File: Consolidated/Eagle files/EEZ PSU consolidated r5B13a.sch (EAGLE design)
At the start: 551 parts, among them IC1 LTC3864EMSE#PBF, IC10 DAC8552IDGKTG4, IC11 ADG465SOT-23, IC12 TS5A9411DCKT, IC13 ADS1120IPWR, IC14 LP339D, IC15 TPD4E002DRL, IC16 TPD2E001DZDR, IC17 ADUM3160BRWZ, IC18 TLC5925IDBQR, IC19 Si8641EC-B-IS1, IC2 LP2951SO8, IC20 SI8651EC-B-IS1, IC21 SI8651EC-B-IS1, IC22 LD1117ADT33TR, IC23 Si8641EC-B-IS1, IC24 PCA21125T/Q900/1,1, IC25 AT25256B-SSHL-B, IC26 W5500, IC27 BC857BS, IC28 TLC555, IC29 SN74LVC08APWR, IC3 TL783CKTTR, IC30 SN74LV1T34DBVR, IC31 TPS3705-33D, IC32 SN74LVC2G02DCTR, IC33 74LVC1G125GW.125, IC34 TPA6205A1DGN, IC4 LTC3260EMSE#PBF, IC5 TL072D, IC6 TL072D, IC7 LTC2050HVCS8#PBF, IC8 MCP23S17-E/SS, IC9 REF5025AIDG4, J1 BS-244DSM-R, J2 1-726388-2, J3 BS-244DSM-G, J4 BS-244DSM-B, J5 BS-244DSM-R, J6 BS-244DSM-B, J7 693072010801, Q1 IRFR5305, Q10 MMBT5401, Q11 MMBT5551, Q12 MMBT5551, Q13 IRLL2705PBF, Q14 IRFR48ZPBF, Q15 IRLML2246TRPBF, Q16 2N7002, Q17 MMBT5551, Q18 MMBT5401, Q19 MMBT5551, Q2 MMBT5401, Q20 MMBT5551, Q21 BTA26-600, Q22 BTA26-600, Q23 IRLL2705PBF, Q24 2N7002, Q25 2N7002, Q26 IRLML2246TRPBF, Q27 IRLML2246TRPBF, Q28 IRLML2246TRPBF, Q29 IRLML2246TRPBF, Q3 2N7002, Q30 2N7002, Q31 IRLML2246TRPBF, Q32 2N7002, Q33 2N7002, Q34 2N7002, Q4 IRFP250N, Q5 BC857C, Q6 BCP56-16.115, Q7 IRFR5305, Q8 BCP56-16.115, Q9 MMBT5401, SW1 A101SYCQ04, SW2 PEC12R-4225F-S0024, SW3 1301.9316, X1 39-30-1039, X10 826629-5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

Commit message: r5B13a Eagle files
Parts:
- removed JP5, JP6, JP7, JP8: 0R-JUMPA, jump-0r-smd:0R-JUMPA
- added C156: 1u, rcl:C-EUC0805
- added R178: 100K, rcl:R-EU_R0805
- R160: value n.c. -> 100K
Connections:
- removed net N$104: JP7-0R.2, LCD1.T_DO
- removed net N$105: JP5-0R.2, LCD1.T_CLK
- removed net N$106: JP6-0R.2, LCD1.T_DIN
- net !MR: now also IC31.!WDO; no longer JP8-0R.1
- net !RESET: now also R160.1
- net +3V3: no longer R160.2
- net GND: now also C156.2, R178.2; no longer IC31.PFI
- net MISO: no longer JP7-0R.1
- net MOSI: no longer JP6-0R.1
- net N$151: now also C156.1, IC31.PFI, R160.2, R178.1; no longer IC31.!WDO, JP8-0R.2
- net N$185: now also IC31.!PFO; no longer JP8-0R.3, R160.1
- net SCLK: no longer JP5-0R.1
- net TOUCH_DIN: now also LCD1.T_DIN; no longer JP6-0R.3
- net TOUCH_DOUT: now also LCD1.T_DO; no longer JP7-0R.3
- net TOUCH_SCLK: now also LCD1.T_CLK; no longer JP5-0R.3
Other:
- note added: "EEZ PSU consolidated r5B13a - Sheet: 3/12"
- note removed: "EEZ PSU consolidated r5B13 - Sheet: 3/12"
- moved on the sheet: C139, C140, D21, IC31, R160

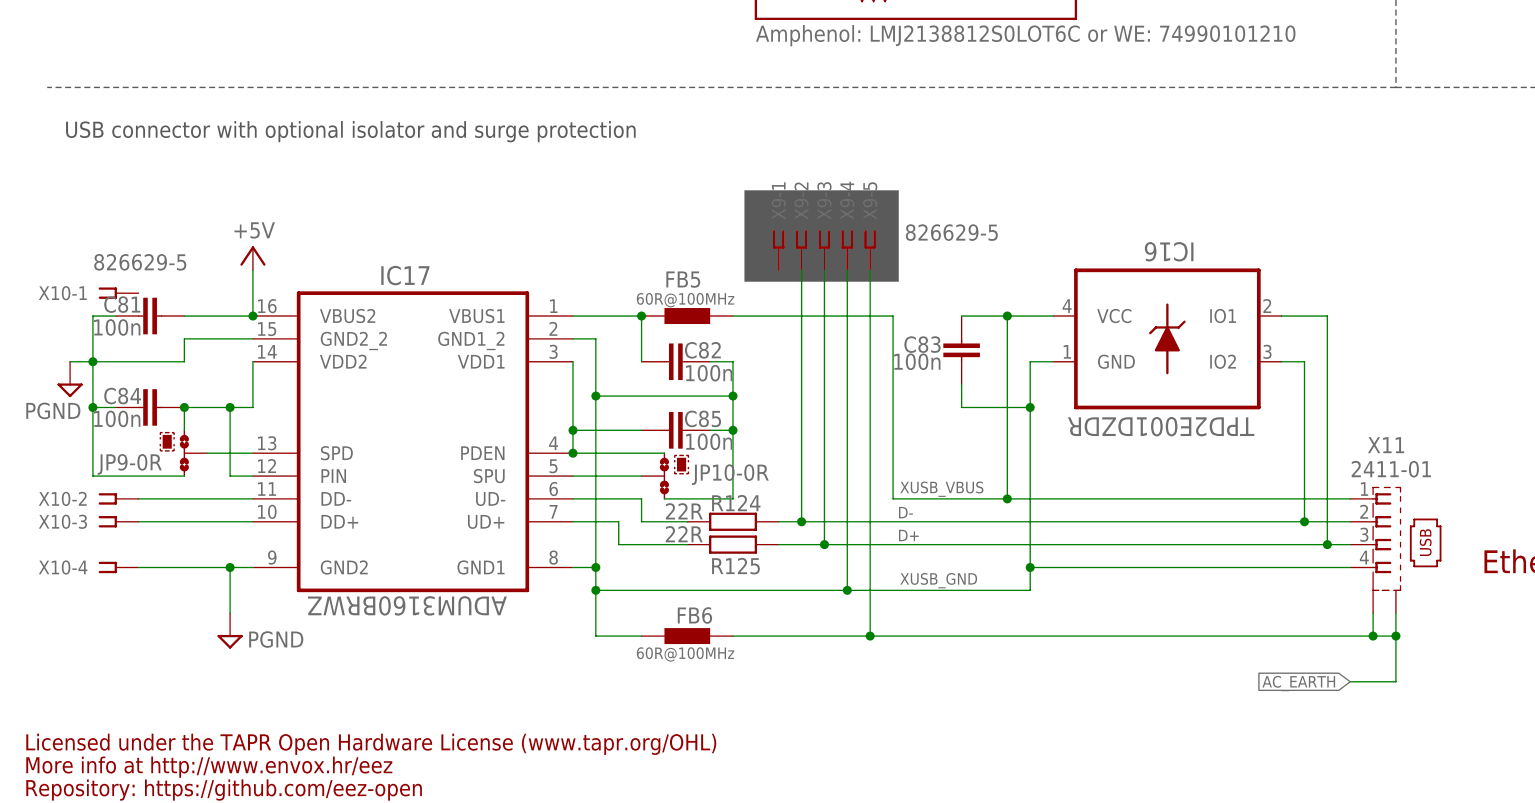
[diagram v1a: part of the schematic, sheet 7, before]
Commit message: JP9, JP10 changed to THT
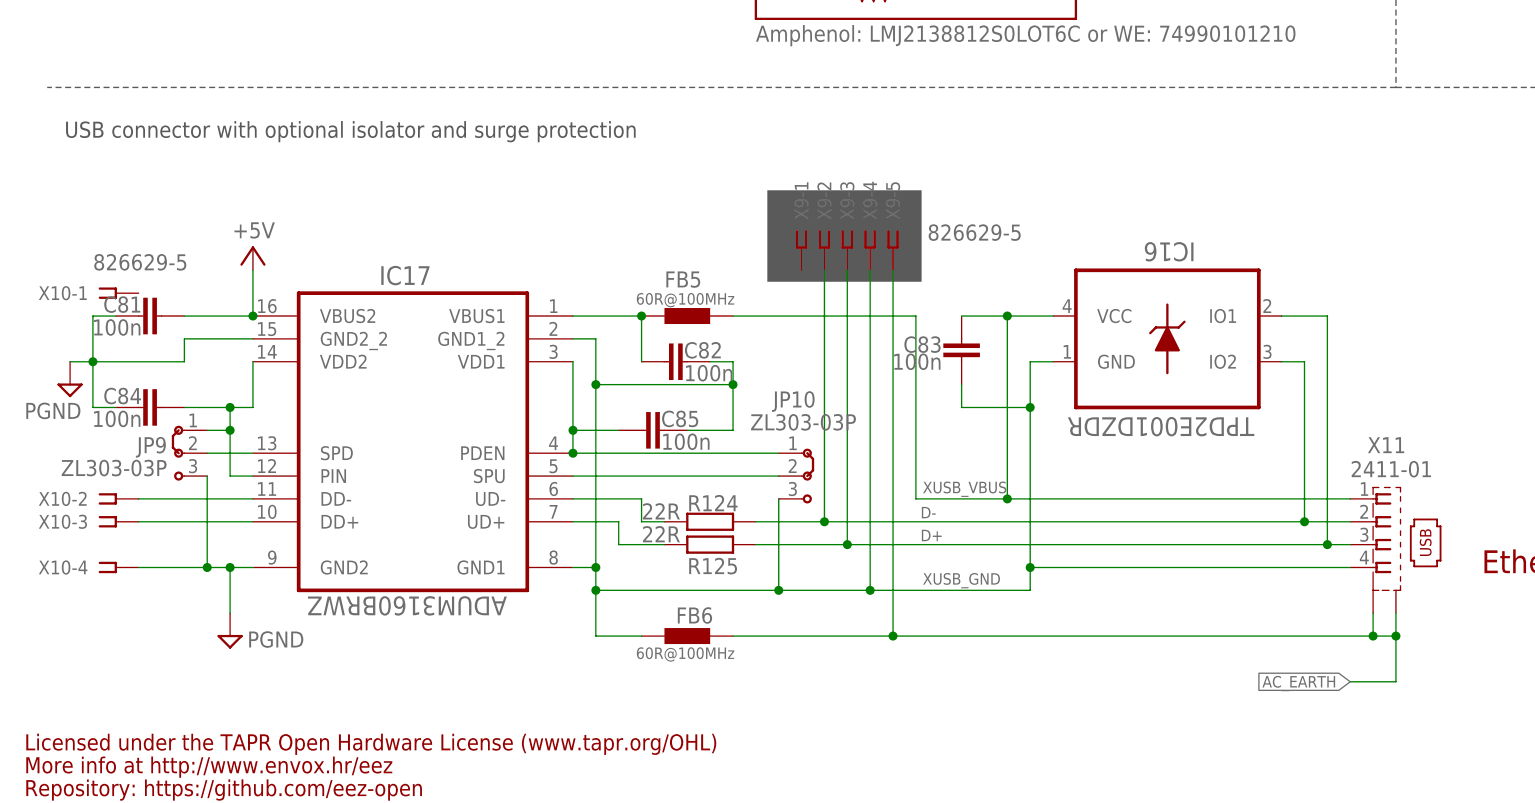
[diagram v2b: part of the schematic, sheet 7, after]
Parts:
- JP10, JP9: value 0R-JUMPA -> ZL303-03P; device jump-0r-smd:0R-JUMPA -> EEZ_Lib1:JUMPER-3PIN2MM
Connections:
- net GND: now also JP9.3; no longer JP9-0R.3
- net N$125: now also JP10.2; no longer JP10-0R.2
- net N$54: now also JP9.2; no longer JP9-0R.2
- net N$87: now also JP10.1; no longer JP10-0R.1
- net N$91: now also JP9.1; no longer JP9-0R.1
- net XUSB_GND: now also JP10.3; no longer JP10-0R.3
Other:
- note added: "1-2"
- note added: "2-3"
- note added: "High"
- note added: "JP9, JP10"
- note added: "Low"
- note added: "USB speed"
- moved on the sheet: C85, R124, R125, X9-1, X9-2, X9-3, X9-4, X9-5

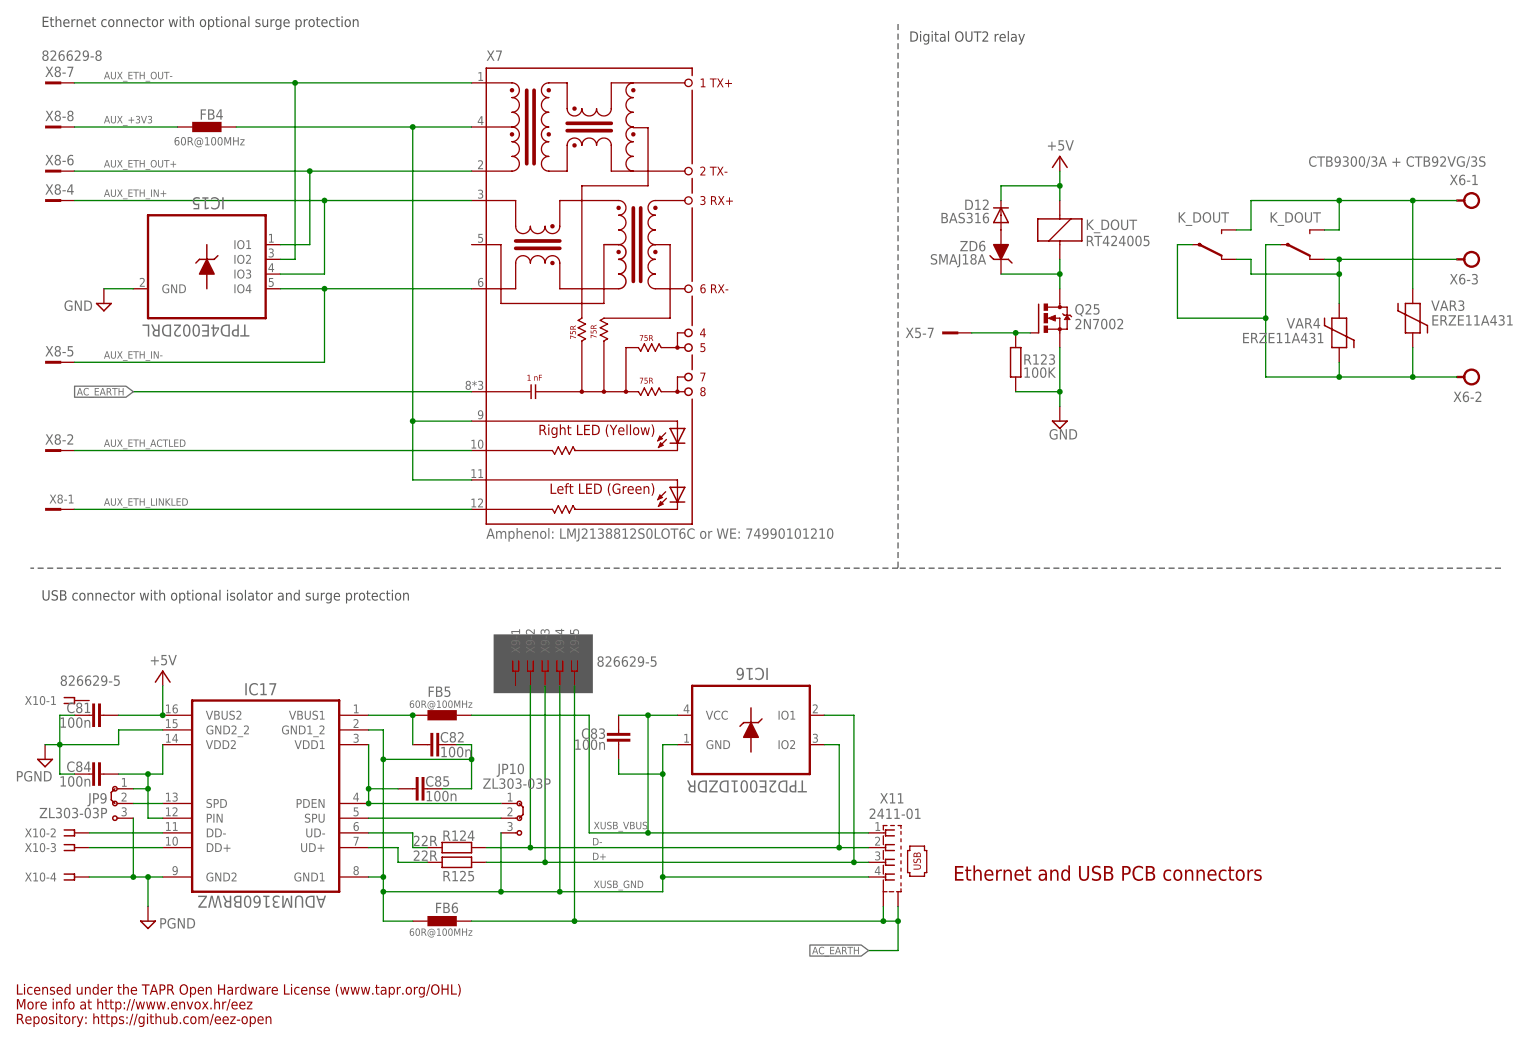
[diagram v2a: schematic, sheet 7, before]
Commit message: X1 holes adjustment
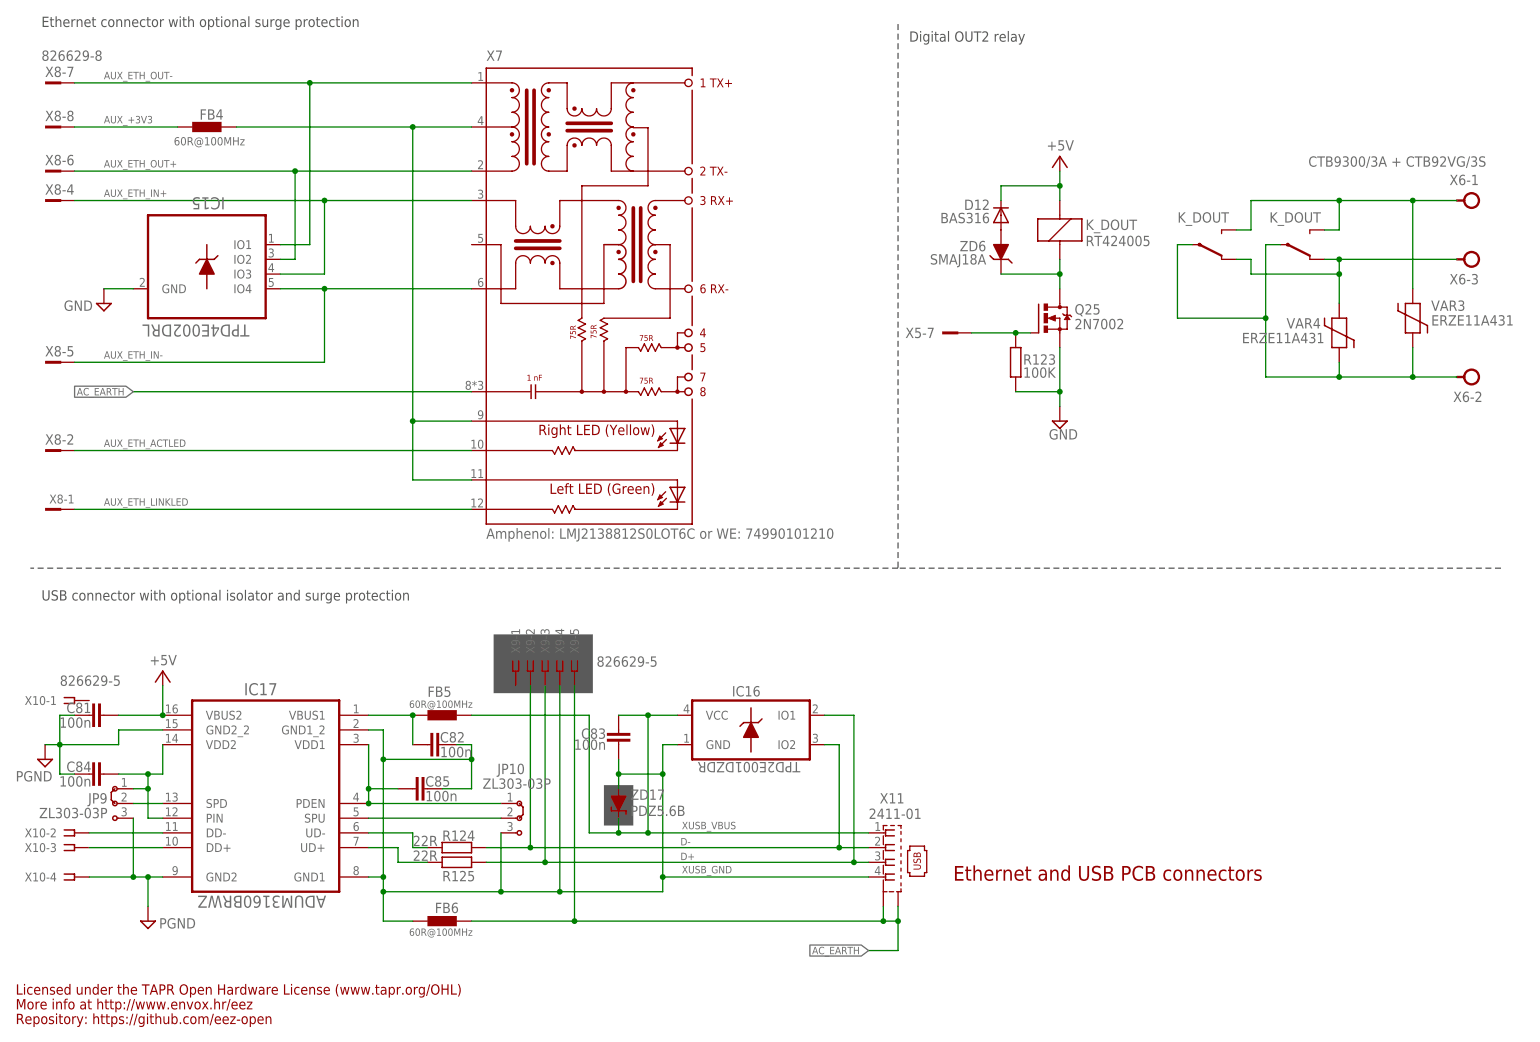
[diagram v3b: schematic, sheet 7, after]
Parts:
- added ZD17: PDZ5.6B, EEZ_Lib1:ZENER-DIODESOD323
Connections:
- net AC_IN1: now also ZD15.A; no longer ZD15.2
- net AC_IN2: now also ZD15.C; no longer ZD15.1
- net AUX_ETH_OUT+: now also IC15.IO2; no longer IC15.IO1
- net AUX_ETH_OUT-: now also IC15.IO1; no longer IC15.IO2
- net DC_OUT: now also ZD1.C; no longer ZD1.1
- net GND: now also ZD1.A; no longer ZD1.2
- net XUSB_GND: now also ZD17.A
- net XUSB_VBUS: now also ZD17.C
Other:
- note added: "Mount Q21 and Q22 on KK1"
- note removed: "Mount Q20 and Q21 on KK1"
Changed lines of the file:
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@@
 <part name="JP9" library="EEZ_Lib1" deviceset="JUMPER-3PIN" device="2MM" value="ZL303-03P"/>
 <part name="JP10" library="EEZ_Lib1" deviceset="JUMPER-3PIN" device="2MM" value="ZL303-03P"/>
+<part name="ZD17" library="EEZ_Lib1" deviceset="ZENER-DIODE" device="SOD323" value="PDZ5.6B"/>
 </parts>
 <sheets>
@@
 </segment>
 <segment>
-<pinref part="ZD1" gate="G$1" pin="2"/>
+<pinref part="ZD1" gate="G$1" pin="A"/>
 <wire x1="114.3" y1="160.02" x2="111.76" y2="160.02" width="0.4064" layer="91"/>
 <wire x1="111.76" y1="160.02" x2="111.76" y2="157.48" width="0.4064" layer="91"/>
@@
 <wire x1="129.54" y1="144.78" x2="124.46" y2="144.78" width="0.4064" layer="91"/>
 <junction x="124.46" y="144.78"/>
-<pinref part="ZD1" gate="G$1" pin="1"/>
+<pinref part="ZD1" gate="G$1" pin="C"/>
 <wire x1="121.92" y1="160.02" x2="124.46" y2="160.02" width="0.4064" layer="91"/>
 <pinref part="L1" gate="-1" pin="2"/>
@@
 <text x="88.265" y="107.95" size="1.778" layer="97" rot="MR180">+12VDC fan control</text>
 <wire x1="86.36" y1="43.18" x2="86.36" y2="109.22" width="0.1524" layer="97" style="shortdash"/>
-<text x="146.05" y="166.37" size="1.6764" layer="103">Mount Q20 and Q21 on KK1</text>
+<text x="146.05" y="166.37" size="1.6764" layer="103">Mount Q21 and Q22 on KK1</text>
 <text x="184.785" y="107.95" size="1.778" layer="97" rot="MR180">Fan sense (tacho out)</text>
 <wire x1="182.88" y1="38.1" x2="182.88" y2="109.22" width="0.1524" layer="97" style="shortdash"/>
@@
 <text x="34.925" y="70.485" size="1.6764" layer="103">USB speed</text>
 <text x="38.1" y="64.77" size="1.6764" layer="103">Low</text>
+<rectangle x1="104.14" y1="36.83" x2="109.22" y2="43.815" layer="97"/>
 </plain>
 <instances>
@@
 </instance>
 <instance part="IC16" gate="A" x="129.54" y="53.34" smashed="yes" rot="MR0">
-<attribute name="NAME" x="126.873" y="64.0588" size="2.0828" layer="95" ratio="10" rot="SMR180"/>
-<attribute name="VALUE" x="118.4148" y="44.6278" size="2.0828" layer="96" ratio="10" rot="SMR180"/>
+<attribute name="NAME" x="126.238" y="59.1312" size="1.778" layer="95" ratio="10" rot="SR0"/>
+<attribute name="VALUE" x="120.3198" y="47.8028" size="1.778" layer="96" ratio="10" rot="SMR180"/>
 </instance>
 <instance part="SUPPLY48" gate="GND" x="17.78" y="127" smashed="yes" rot="MR0">
@@
 <attribute name="VALUE" x="83.185" y="43.18" size="1.778" layer="96"/>
 </instance>
+<instance part="ZD17" gate="G$1" x="106.68" y="40.64" smashed="yes" rot="R270">
+<attribute name="NAME" x="108.712" y="41.275" size="1.778" layer="95"/>
+<attribute name="VALUE" x="108.712" y="38.481" size="1.778" layer="96"/>
+</instance>
 </instances>
 <busses>
@@
 <net name="D-" class="0">
 <segment>
-<label x="102.108" y="33.401" size="1.27" layer="102"/>
+<label x="117.348" y="33.401" size="1.27" layer="102"/>
 <pinref part="R124" gate="G$1" pin="1"/>
 <wire x1="83.82" y1="33.02" x2="91.44" y2="33.02" width="0.1524" layer="91"/>
@@
 <net name="D+" class="0">
 <segment>
-<label x="102.108" y="30.861" size="1.27" layer="102"/>
+<label x="117.348" y="30.861" size="1.27" layer="102"/>
 <pinref part="R125" gate="G$1" pin="1"/>
 <wire x1="83.82" y1="30.48" x2="93.98" y2="30.48" width="0.1524" layer="91"/>
@@
 <net name="XUSB_VBUS" class="0">
 <segment>
-<label x="102.362" y="36.195" size="1.27" layer="102"/>
+<label x="117.602" y="36.195" size="1.27" layer="102"/>
 <pinref part="FB5" gate="G$1" pin="1"/>
 <pinref part="X11" gate="G$1" pin="1"/>
@@
 <wire x1="111.76" y1="55.88" x2="106.68" y2="55.88" width="0.1524" layer="91"/>
 <junction x="111.76" y="55.88"/>
-<wire x1="111.76" y1="35.56" x2="101.6" y2="35.56" width="0.1524" layer="91"/>
+<wire x1="111.76" y1="35.56" x2="106.68" y2="35.56" width="0.1524" layer="91"/>
+<wire x1="106.68" y1="35.56" x2="101.6" y2="35.56" width="0.1524" layer="91"/>
 <wire x1="101.6" y1="35.56" x2="101.6" y2="55.88" width="0.1524" layer="91"/>
 <pinref part="C83" gate="G$1" pin="2"/>
+<wire x1="106.68" y1="38.1" x2="106.68" y2="35.56" width="0.1524" layer="91"/>
+<junction x="106.68" y="35.56"/>
+<pinref part="ZD17" gate="G$1" pin="C"/>
 </segment>
 </net>
@@
 <junction x="66.04" y="48.26"/>
 <wire x1="66.04" y1="20.32" x2="66.04" y2="25.4" width="0.1524" layer="91"/>
-<label x="102.362" y="26.035" size="1.27" layer="102"/>
+<label x="117.602" y="28.575" size="1.27" layer="102"/>
 <pinref part="X9" gate="-4" pin="1"/>
 <pinref part="X11" gate="G$1" pin="4"/>
@@
 <wire x1="86.36" y1="35.56" x2="86.36" y2="25.4" width="0.1524" layer="91"/>
 <junction x="86.36" y="25.4"/>
+<wire x1="106.68" y1="43.18" x2="106.68" y2="45.72" width="0.1524" layer="91"/>
+<junction x="106.68" y="45.72"/>
+<pinref part="ZD17" gate="G$1" pin="A"/>
 </segment>
 </net>
 <net name="AUX_ETH_OUT-" class="0">
 <segment>
-<wire x1="81.28" y1="165.1" x2="50.8" y2="165.1" width="0.1524" layer="91"/>
 <pinref part="X7" gate="G$1" pin="TD+"/>
-<wire x1="50.8" y1="165.1" x2="12.7" y2="165.1" width="0.1524" layer="91"/>
-<wire x1="50.8" y1="134.62" x2="50.8" y2="165.1" width="0.1524" layer="91"/>
-<junction x="50.8" y="165.1"/>
+<wire x1="81.28" y1="165.1" x2="53.34" y2="165.1" width="0.1524" layer="91"/>
 <label x="17.78" y="165.735" size="1.27" layer="102"/>
 <pinref part="X8" gate="-7" pin="1"/>
-<pinref part="IC15" gate="A" pin="IO2"/>
-<wire x1="48.26" y1="134.62" x2="50.8" y2="134.62" width="0.1524" layer="91"/>
+<pinref part="IC15" gate="A" pin="IO1"/>
+<wire x1="53.34" y1="165.1" x2="12.7" y2="165.1" width="0.1524" layer="91"/>
+<wire x1="48.26" y1="137.16" x2="53.34" y2="137.16" width="0.1524" layer="91"/>
+<wire x1="53.34" y1="137.16" x2="53.34" y2="165.1" width="0.1524" layer="91"/>
+<junction x="53.34" y="165.1"/>
 </segment>
 </net>
@@
 <segment>
 <pinref part="X7" gate="G$1" pin="TD-"/>
-<wire x1="12.7" y1="149.86" x2="53.34" y2="149.86" width="0.1524" layer="91"/>
-<wire x1="53.34" y1="149.86" x2="81.28" y2="149.86" width="0.1524" layer="91"/>
-<junction x="53.34" y="149.86"/>
+<wire x1="12.7" y1="149.86" x2="50.8" y2="149.86" width="0.1524" layer="91"/>
 <label x="17.78" y="150.495" size="1.27" layer="102"/>
 <pinref part="X8" gate="-6" pin="1"/>
-<pinref part="IC15" gate="A" pin="IO1"/>
-<wire x1="53.34" y1="137.16" x2="53.34" y2="149.86" width="0.1524" layer="91"/>
-<wire x1="48.26" y1="137.16" x2="53.34" y2="137.16" width="0.1524" layer="91"/>
+<pinref part="IC15" gate="A" pin="IO2"/>
+<wire x1="50.8" y1="149.86" x2="81.28" y2="149.86" width="0.1524" layer="91"/>
+<wire x1="48.26" y1="134.62" x2="50.8" y2="134.62" width="0.1524" layer="91"/>
+<wire x1="50.8" y1="134.62" x2="50.8" y2="149.86" width="0.1524" layer="91"/>
+<junction x="50.8" y="149.86"/>
 </segment>
 </net>
@@
 <pinref part="R163" gate="G$1" pin="1"/>
 <pinref part="IC30" gate="A" pin="I"/>
+<wire x1="162.56" y1="86.36" x2="170.18" y2="86.36" width="0.1524" layer="91"/>
 </segment>
 </net>
@@
 </instance>
 <instance part="R171" gate="G$1" x="142.24" y="76.2" smashed="yes" rot="MR0">
-<attribute name="NAME" x="139.7" y="74.7014" size="1.778" layer="95" rot="MR180"/>
-<attribute name="VALUE" x="139.7" y="79.502" size="1.778" layer="96" rot="MR180"/>
+<attribute name="NAME" x="139.7" y="79.1464" size="1.778" layer="95" rot="MR180"/>
+<attribute name="VALUE" x="140.97" y="74.422" size="1.778" layer="96" rot="MR180"/>
 </instance>
 <instance part="R170" gate="G$1" x="129.54" y="76.2" smashed="yes" rot="MR0">
-<attribute name="NAME" x="127" y="74.7014" size="1.778" layer="95" rot="MR180"/>
-<attribute name="VALUE" x="127" y="79.502" size="1.778" layer="96" rot="MR180"/>
+<attribute name="NAME" x="126.365" y="79.1464" size="1.778" layer="95" rot="MR180"/>
+<attribute name="VALUE" x="127.635" y="74.422" size="1.778" layer="96" rot="MR180"/>
 </instance>
 <instance part="C152" gate="G$1" x="137.16" y="68.58" smashed="yes">
@@
 <wire x1="50.8" y1="154.94" x2="50.8" y2="149.86" width="0.4064" layer="91"/>
 <junction x="50.8" y="144.78"/>
-<pinref part="ZD15" gate="G$1" pin="1"/>
+<pinref part="ZD15" gate="G$1" pin="C"/>
 <wire x1="50.8" y1="149.86" x2="50.8" y2="144.78" width="0.4064" layer="91"/>
 <wire x1="33.02" y1="142.24" x2="33.02" y2="154.94" width="0.4064" layer="91"/>
@@
 <wire x1="50.8" y1="124.46" x2="50.8" y2="127" width="0.4064" layer="91"/>
 <junction x="50.8" y="127"/>
-<pinref part="ZD15" gate="G$1" pin="2"/>
+<pinref part="ZD15" gate="G$1" pin="A"/>
 <wire x1="33.02" y1="134.62" x2="33.02" y2="124.46" width="0.4064" layer="91"/>
 <label x="16.51" y="125.095" size="1.27" layer="102"/>
